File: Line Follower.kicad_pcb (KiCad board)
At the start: 4 copper layers, 100 x 70 mm, 13 parts, among them J1 Conn_01x11, J2 Conn_01x08, J3 Conn_01x04, J4 Conn_01x06, J5 Conn_01x06, U1 Teensy4.1, U2 D42V55F5 5V Voltage Regulator, U3 TB67H420FTG Dual Motor Driver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, U4 Big MOSFET Slide Switch with 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

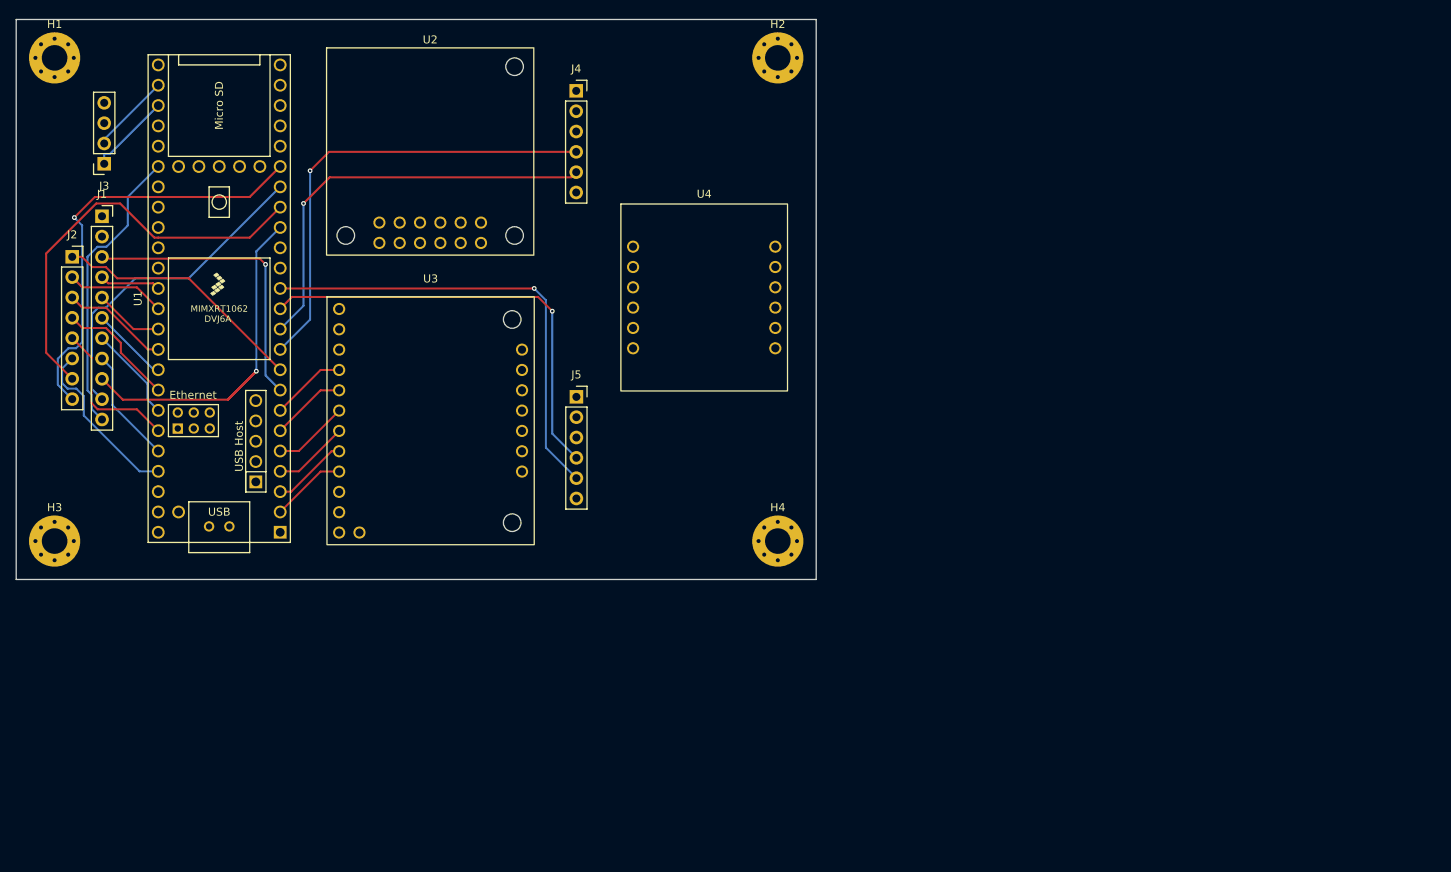
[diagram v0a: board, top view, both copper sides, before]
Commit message: Add PCB routing rules and lock files for Line Follower project
- Created a new freerouting.rules file with detailed autorouting settings, layer rules, via definitions, and clearance classes for the PCB design.
- Added lock files for both the PCB and schematic to track user session information.
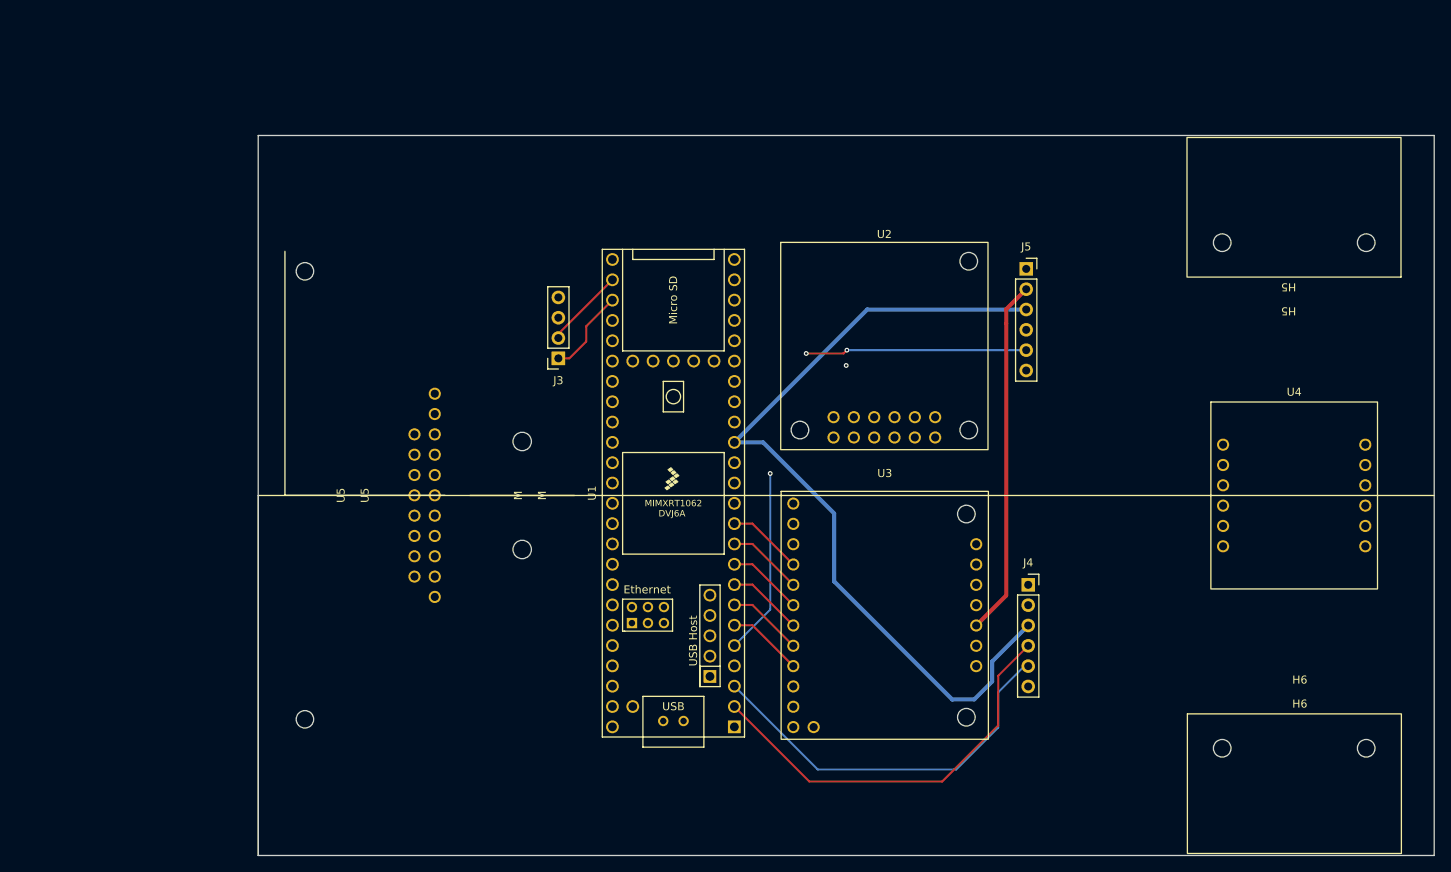
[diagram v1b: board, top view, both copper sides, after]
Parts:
- removed H1, H2, H3, H4: MountingHole_Pad, MountingHole:MountingHole_3.2mm_M3_Pad_Via
- removed J1: Conn_01x11, Connector_PinSocket_2.54mm:PinSocket_1x11_P2.54mm_Vertical
- removed J2: Conn_01x08, Connector_PinSocket_2.54mm:PinSocket_1x08_P2.54mm_Vertical
- added H5: ~, Pololu:Pololu Extended Motor Bracket, F.Cu at (195.5, 56.0)
- added H6: ~, Pololu:Pololu Extended Motor Bracket, F.Cu at (195.5, 128.0)
- added M: Pololu Ball Castor, Pololu:Pololu Ball Castor, F.Cu at (99.0, 92.0)
- added U5: QTRX-HD-15A, Pololu:QTRX-HD-15A, F.Cu at (89.3, 122.5)
- moved J4 83.7 mm to (162.2, 103.2)
- moved U4 77.8 mm to (185.3, 103.4)
- moved U3 61.8 mm to (131.6, 122.2)
- moved U1 61.8 mm to (117.9, 91.7)
- moved J3 61.8 mm to (103.5, 74.9)
- moved U2 61.8 mm to (131.6, 86.0)
- moved J5 58.5 mm to (162.0, 63.7)
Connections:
- U1 pad 10: /ENCODER1_A -> /M1INB
- U1 pad 11: /ENCODER1_B -> /M1INA
- U1 pad 12: /ENCODER2_A -> /QTRXODD
- U1 pad 13: /ENCODER2_B -> /QTRXEVN
- U1 pad 2: /M2PWM -> /ENCODER1_A
- U1 pad 3: /M2INB -> /ENCODER1_B
- U1 pad 4: /M2INA -> /ENCODER2_A
- U1 pad 46: +3.3V -> +3.3V1
- U1 pad 5: /M1PWM -> /ENCODER2_B
- U1 pad 6: /M1INB -> /M2PWM
- U1 pad 7: /M1INA -> /M2INB
- U1 pad 8: /QTRXODD -> /M2INA
- U1 pad 9: /QTRXEVN -> /M1PWM
- U4 pad 3: GND -> unconnected-(U4-GND-Pad3)
- U4 pad 4: GND -> unconnected-(U4-GND-Pad4)
- U4 pad 8: unconnected-(U4-VOUT-Pad8) -> +12V
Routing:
- net +3.3V: track 308.4 -> 103.7 mm
- net /M1B: track 97.5 -> 8.60 mm
- net /M1A: track 100.1 -> 12.9 mm
- net /QTRX14: track 54.0 -> 0.00 mm, vias 1 -> 0
- net /QTRX12: track 52.2 -> 0.00 mm
- net /QTRX11: track 51.1 -> 0.00 mm, vias 1 -> 0
- net +12V: track 60.6 -> 17.6 mm
- net /QTRX13: track 41.3 -> 0.00 mm
- net /QTRXODD: track 37.3 -> 0.00 mm, vias 1 -> 0
- net /M2B: track 7.51 -> 44.6 mm
- net /M2A: track 7.51 -> 44.6 mm
- net /QTRX15: track 36.7 -> 0.00 mm
- net /QTRXEVN: track 31.8 -> 0.00 mm
- net /QTRX10: track 21.6 -> 0.00 mm
- net /QTRX8: track 18.9 -> 0.00 mm
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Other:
- board size 100 x 70 mm -> 147 x 90 mm
